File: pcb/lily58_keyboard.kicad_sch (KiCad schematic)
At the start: 2 parts, among them U2 ESP32-WROOM-32

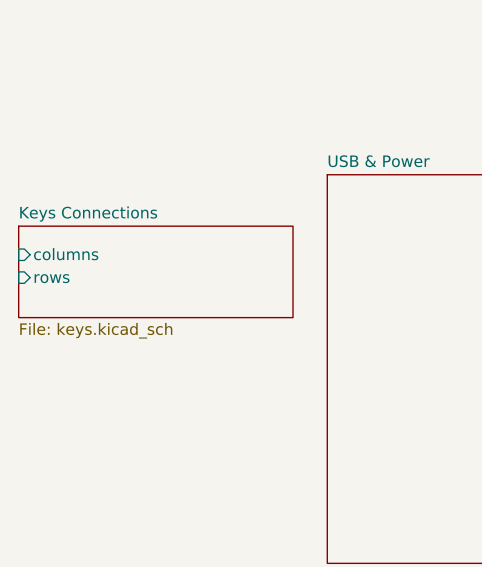
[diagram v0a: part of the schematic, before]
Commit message: USB 3.1 Type C com PD configurado
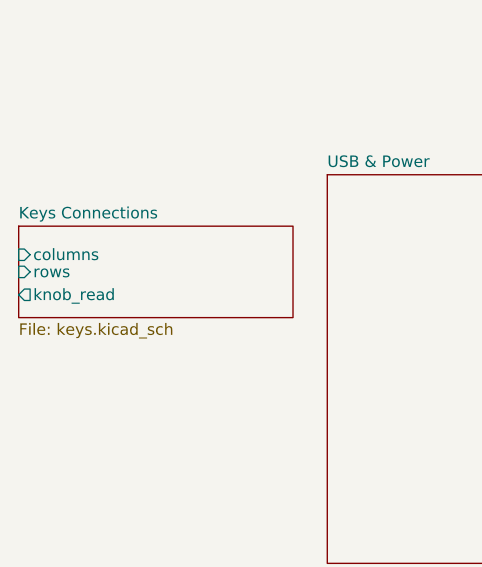
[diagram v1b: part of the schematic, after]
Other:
- sheet Keys Connections ports: added knob_read; removed none
- title: (none) -> バングー Keyboard Schematic
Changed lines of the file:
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@@
 (kicad_sch (version 20230121) (generator eeschema)
   (paper "A4")
+  (title_block
+    (title "バングー Keyboard Schematic")
+    (date "2024-01-20")
+  )
   (symbol (lib_id "Display_Graphic:OLED-128O064D") (at 212.09 69.85 0) (unit 1)
     (in_bom yes) (on_board yes) (dnp no) (fields_autoplaced)
@@
       (effects (font (size 1.27 1.27)) (justify left top))
     )
-    (pin "rows" input (at 28.575 154.305 180)
+    (pin "rows" input (at 28.575 153.67 180)
       (effects (font (size 1.27 1.27)) (justify left))
     )
@@
       (effects (font (size 1.27 1.27)) (justify left))
     )
+    (pin "knob_read" output (at 28.575 156.21 180)
+      (effects (font (size 1.27 1.27)) (justify left))
+    )
